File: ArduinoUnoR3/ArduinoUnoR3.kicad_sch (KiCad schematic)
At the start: 6 parts, among them U1 ATmega16U2-A, U2 LMV358

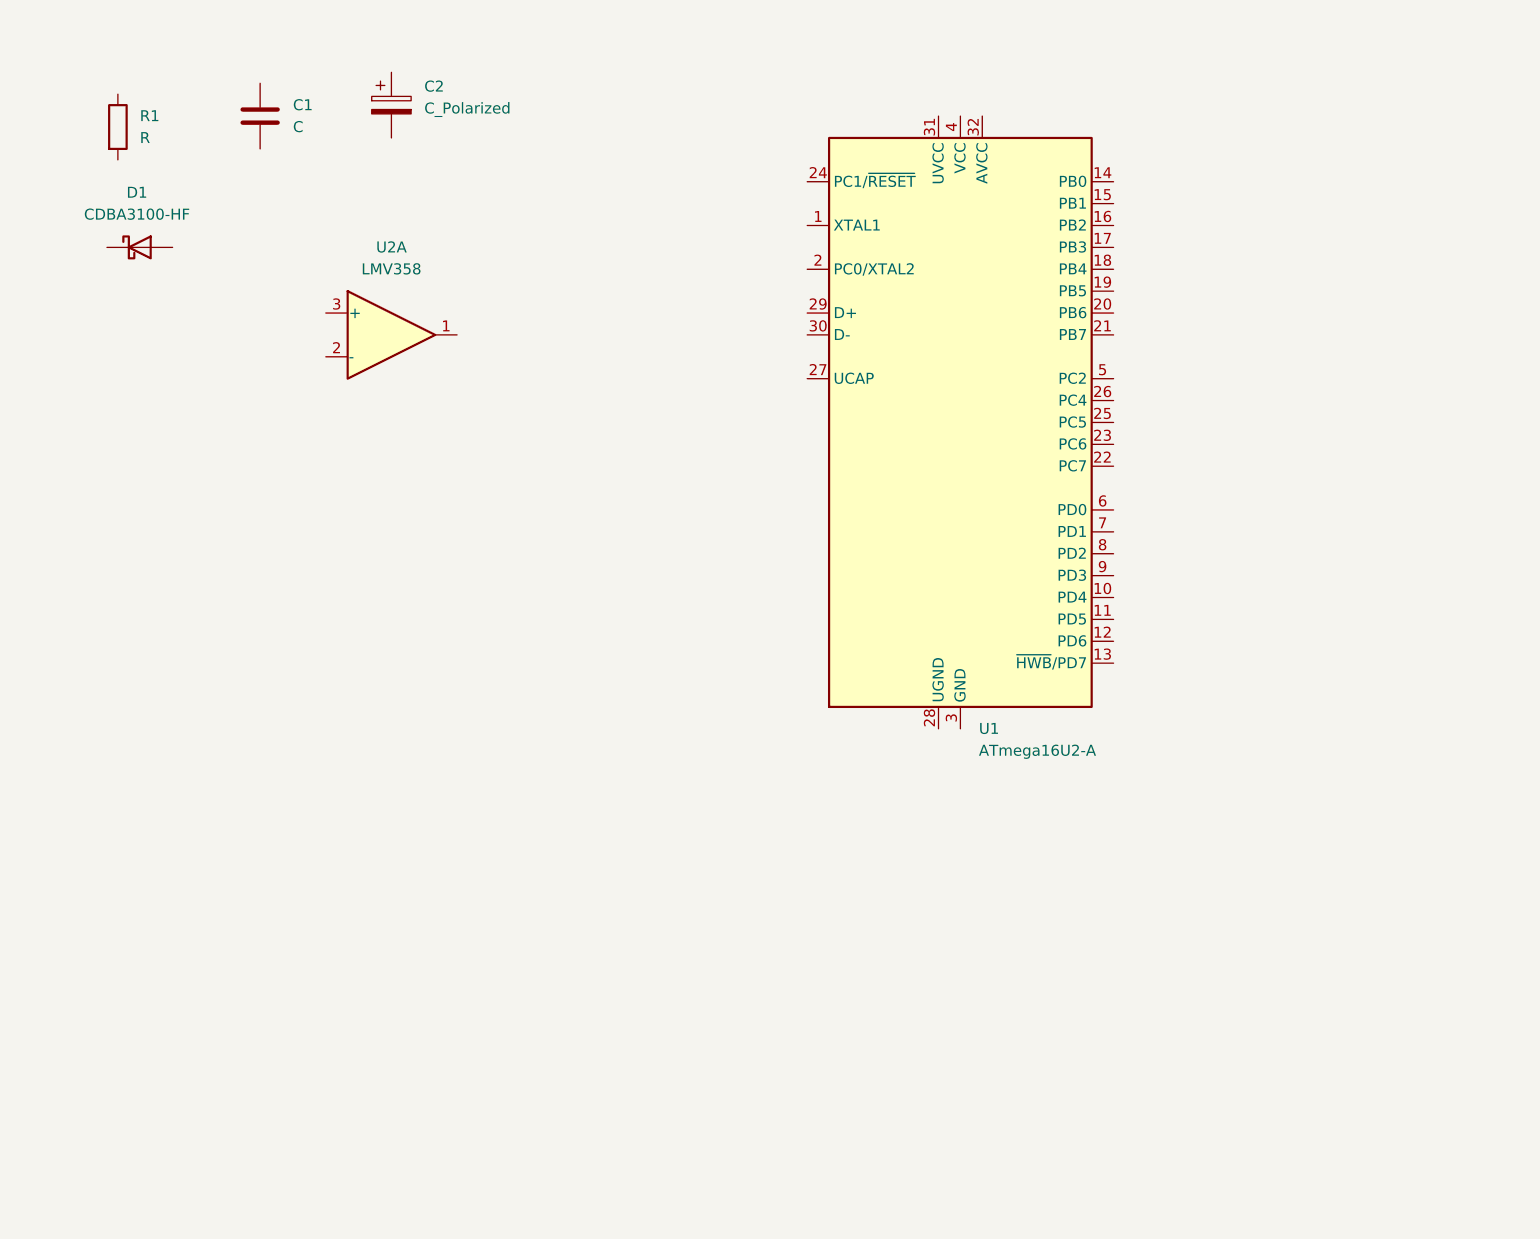
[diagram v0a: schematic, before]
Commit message: Completed the schematic design for ATMEGA16U2-A
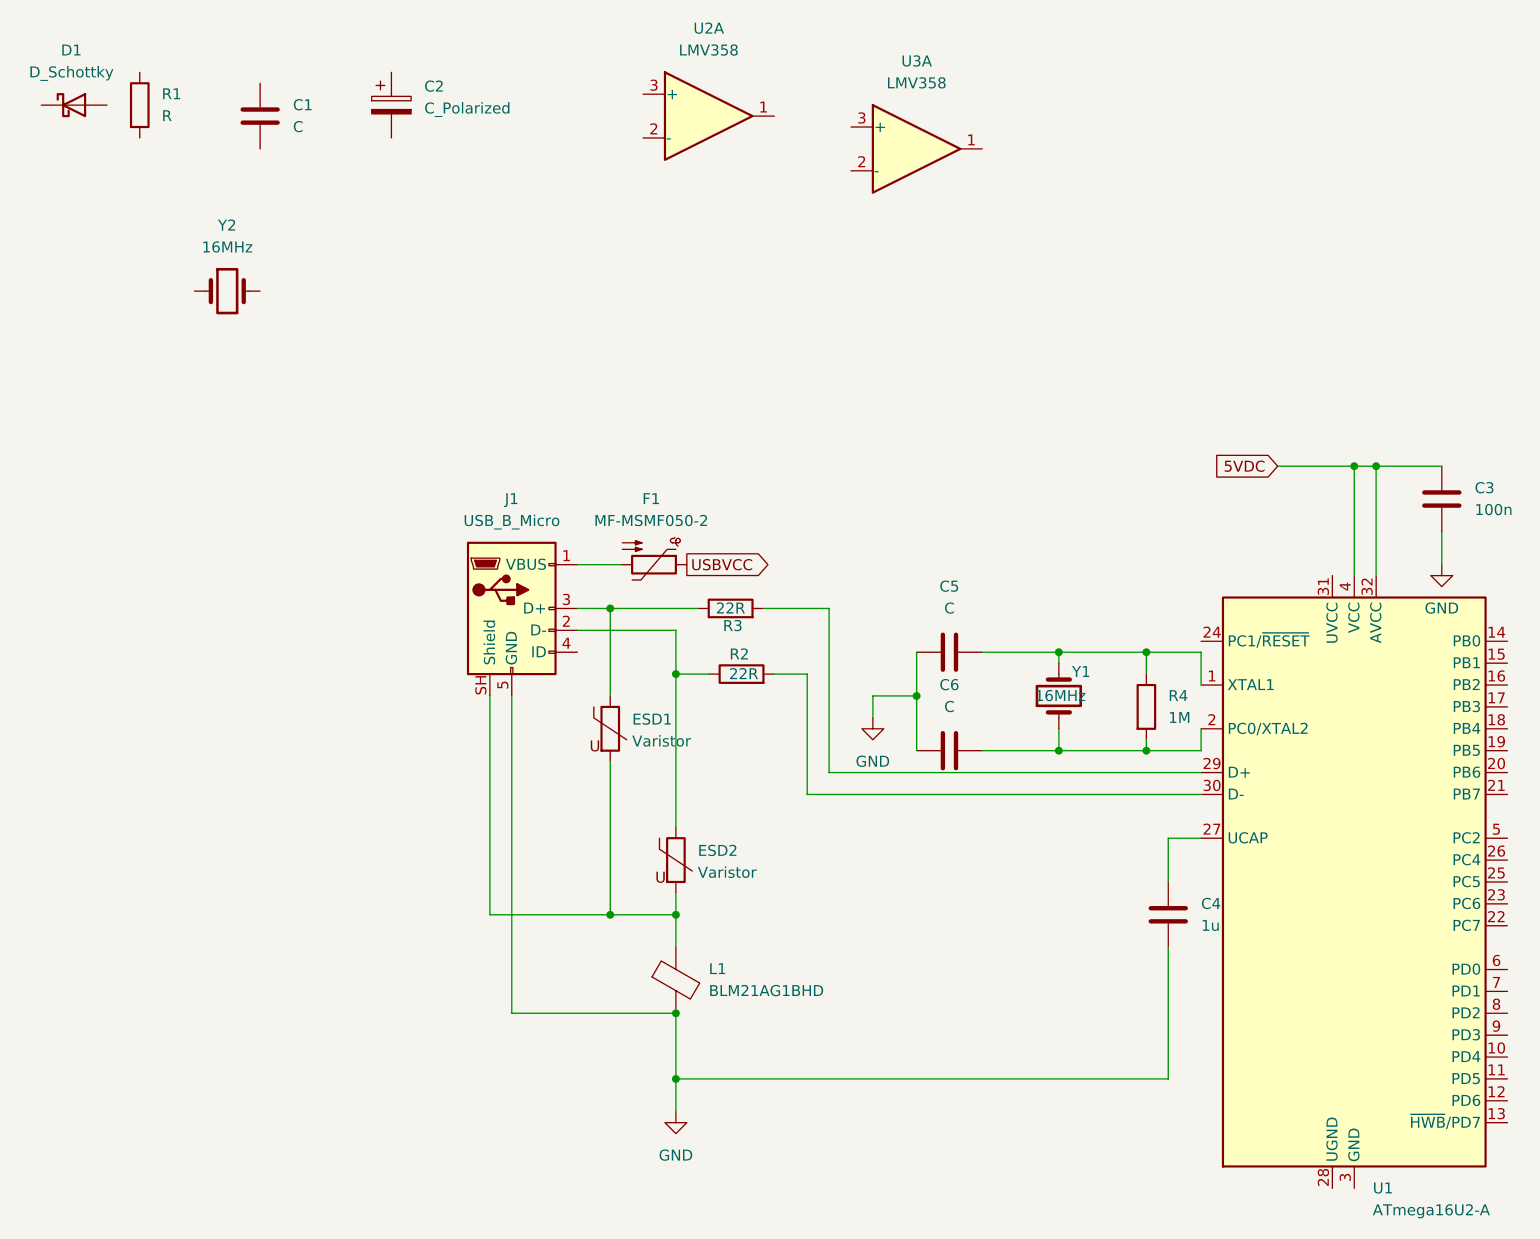
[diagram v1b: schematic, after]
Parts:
- removed D1: CDBA3100-HF, Diode_SMD:D_SMA, symbol Diode:CDBA3100-HF
- added C3: 100n, Capacitor_SMD:C_0603_1608Metric, symbol Device:C
- added C4: 1u, Capacitor_SMD:C_0603_1608Metric, symbol Device:C
- added C5, C6: C, Capacitor_SMD:C_0603_1608Metric, symbol Device:C
- added D1: D_Schottky, Diode_SMD:D_0603_1608Metric, symbol Device:D_Schottky
- added ESD1, ESD2: Varistor, symbol Device:Varistor
- added F1: MF-MSMF050-2, symbol Device:Thermistor_PTC
- added J1: USB_B_Micro, symbol Connector:USB_B_Micro
- added L1: BLM21AG1BHD, symbol Device:FerriteBead
- added R2, R3: 22R, Resistor_SMD:R_0603_1608Metric, symbol Device:R
- added R4: 1M, Resistor_SMD:R_0603_1608Metric, symbol Device:R
- added U3: LMV358, symbol Amplifier_Operational:LMV358
- added Y1, Y2: 16MHz, symbol Device:Crystal
- C1, C2: footprint Capacitor_THT:CP_Radial_D5.0mm_P2.00mm -> Capacitor_SMD:C_0603_1608Metric
- R1: footprint Resistor_THT:R_Axial_DIN0204_L3.6mm_D1.6mm_P7.62mm_Horizontal -> Resistor_SMD:R_0603_1608Metric
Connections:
- net at U1.1 (XTAL1): now also C5.2, R4.1, Y1.2
- net at U1.2 (PC0/XTAL2): now also C6.2, R4.2, Y1.1
- net at U1.27 (UCAP): now also C4.1
- net at U1.29 (D+): now also R3.2
- net at U1.30 (D-): now also R2.2
- net 5VDC: now reaches U1.32 (AVCC)
- net 5VDC: now also U1.4 (VCC), C3.1
- new net: ESD1.1, J1.3 (D+), R3.1
- new net: F1.2, J1.1 (VBUS)
- new net: ESD1.2, ESD2.2, J1.SH (Shield), L1.1
- new net: ESD2.1, J1.2 (D-), R2.1
- new net GND: C3.2, C4.2, C5.1, C6.1, J1.5 (GND), L1.2
- new net USBVCC: F1.1
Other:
- company: (none) -> Denoe
- title: (none) -> ArduinoUnoR3
- moved on the sheet: R1, U1, U2A

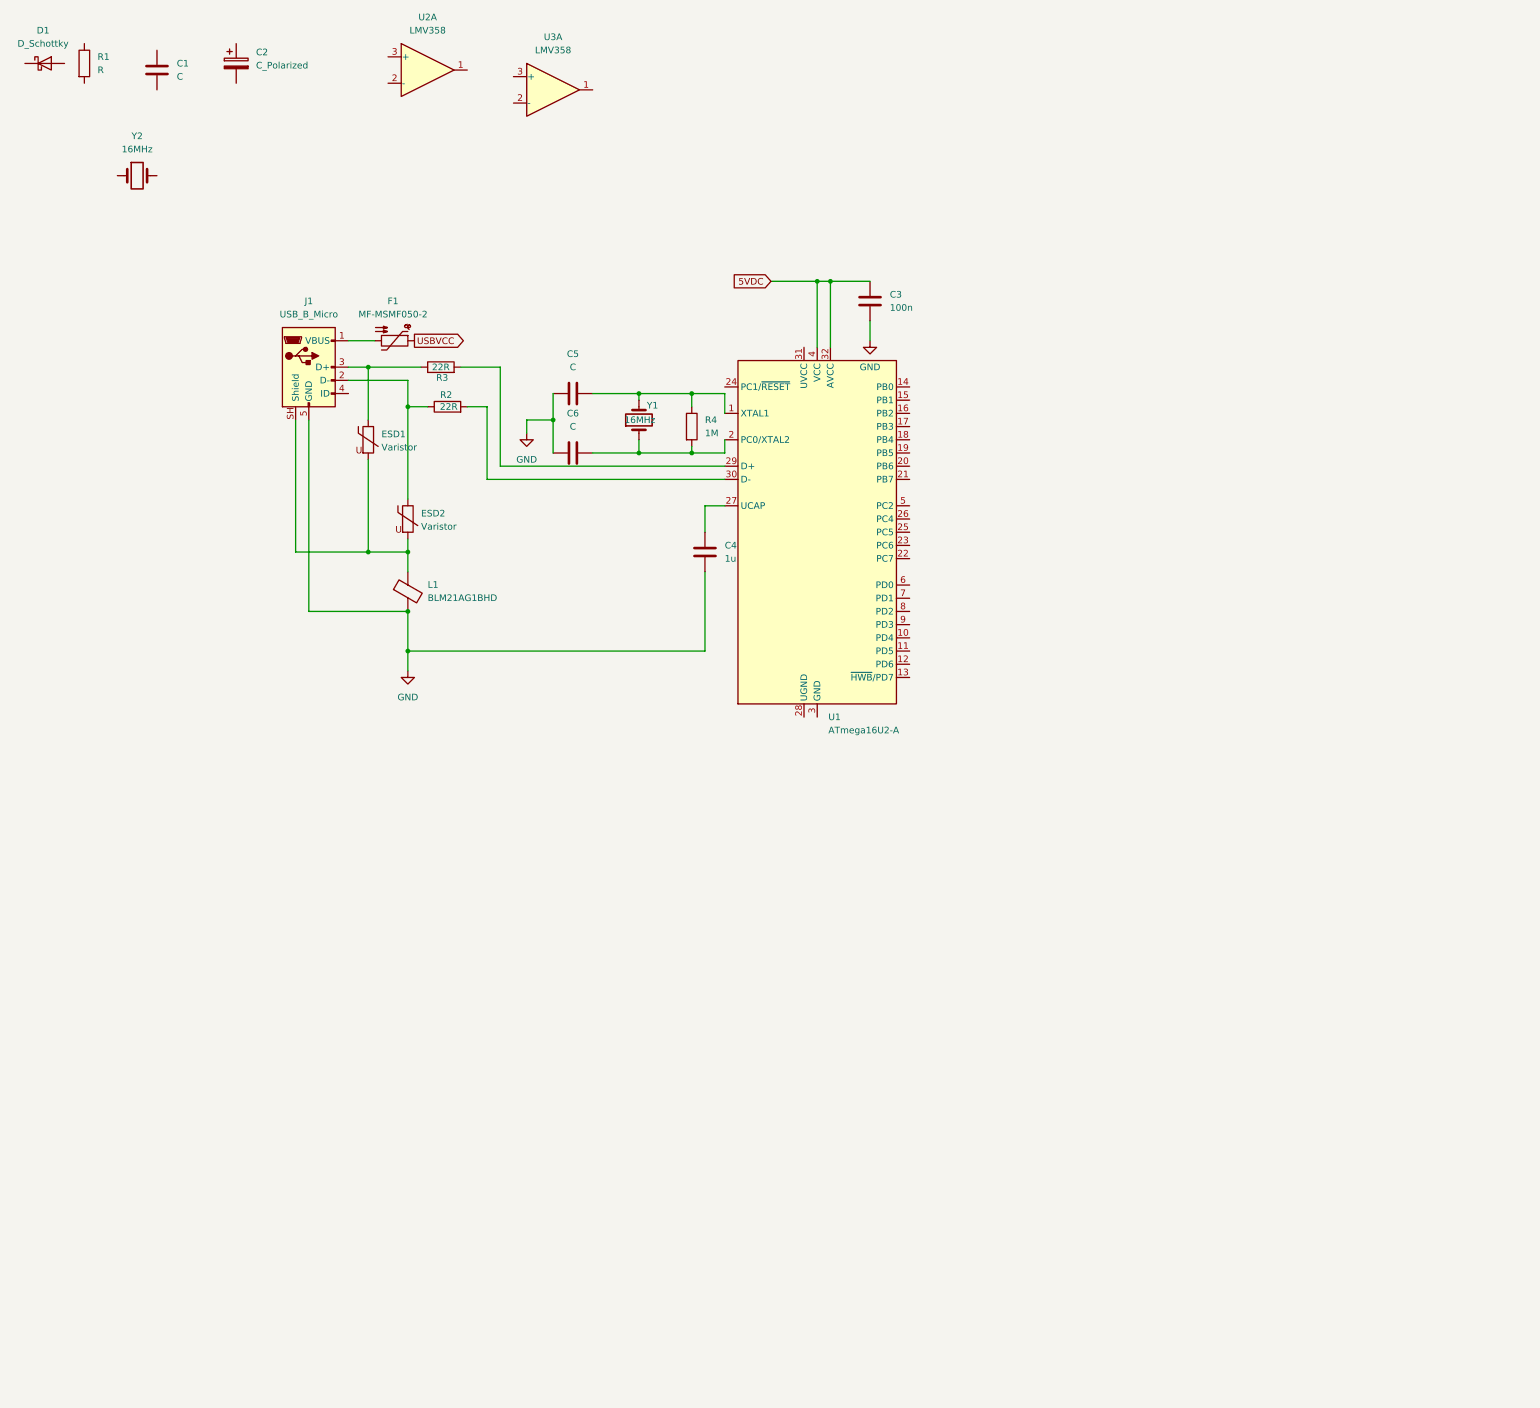
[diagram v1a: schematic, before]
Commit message: Added ATMEGA328PB-A to our schematic files
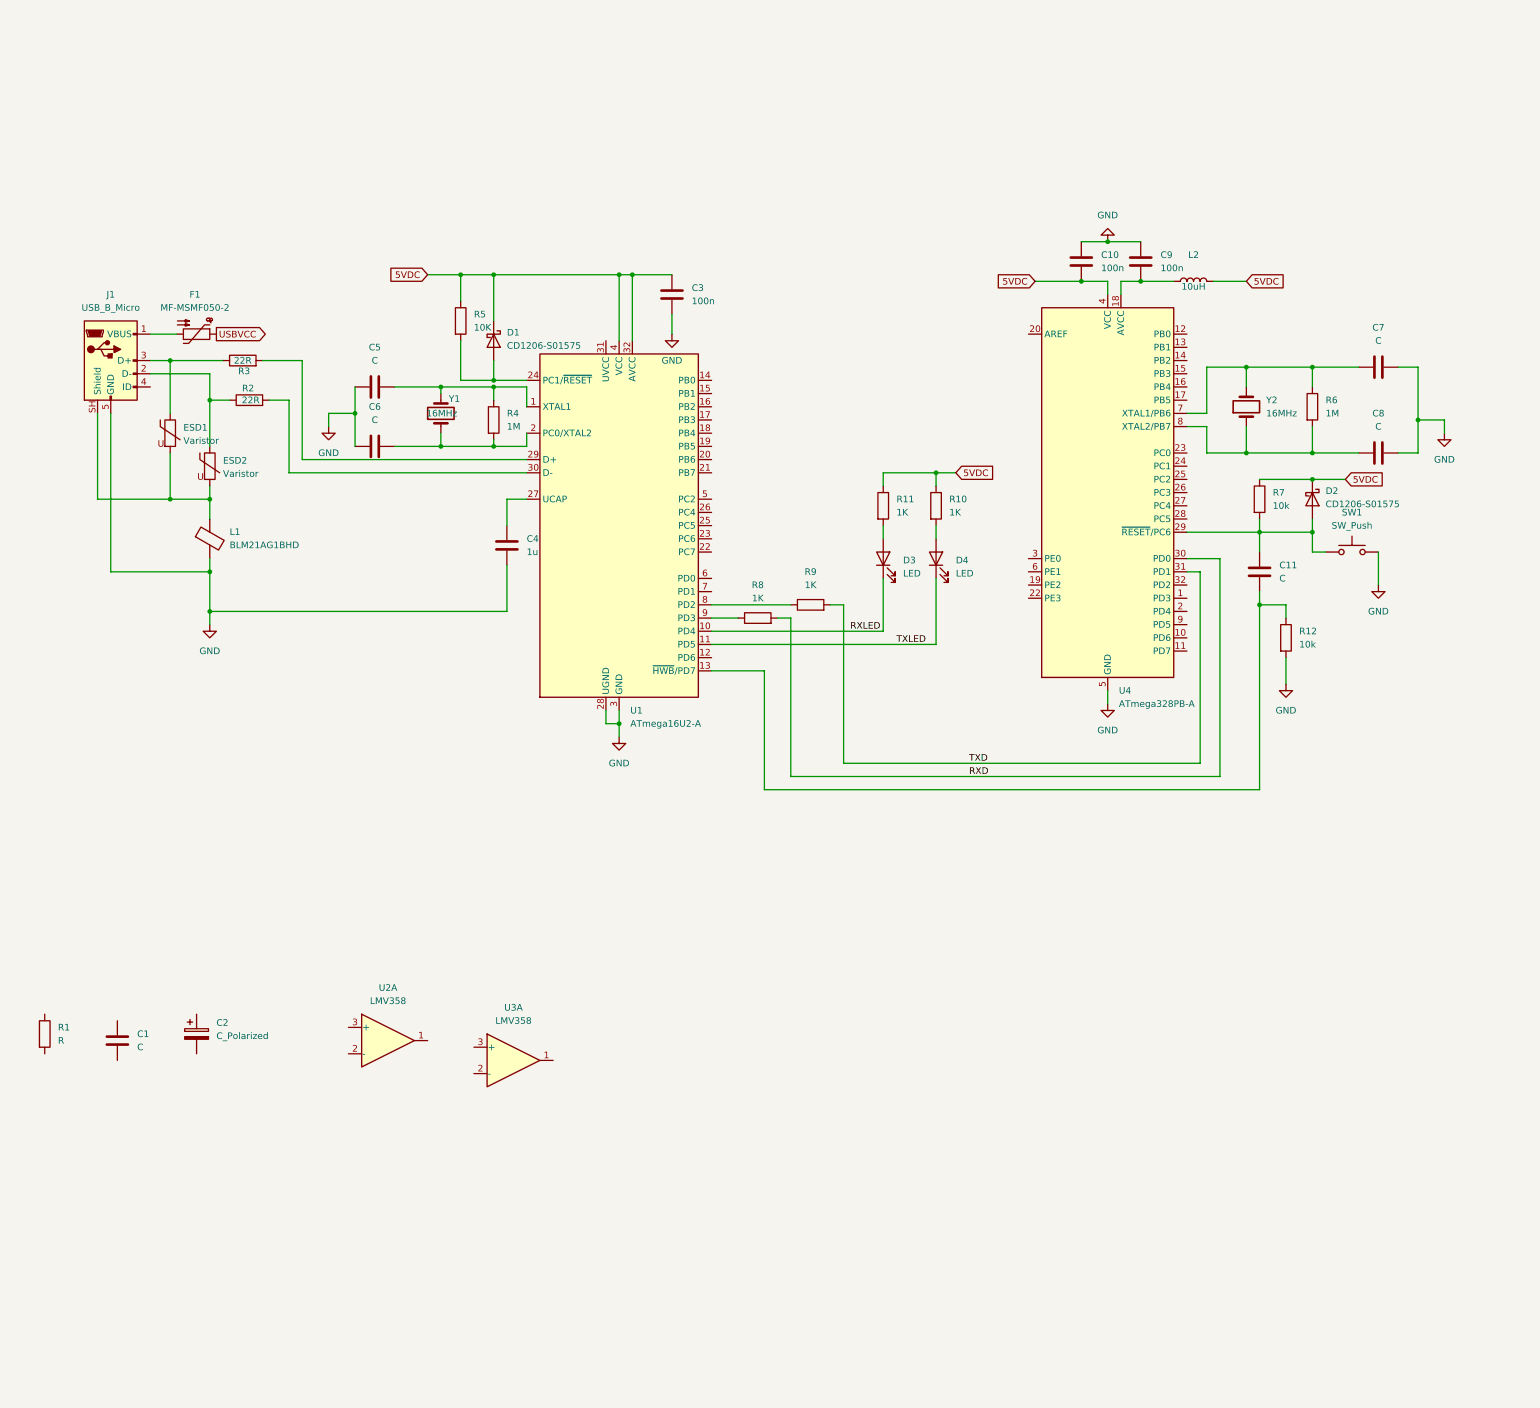
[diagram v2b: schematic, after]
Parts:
- added C10, C9: 100n, Capacitor_SMD:C_0603_1608Metric, symbol Device:C
- added C11, C7, C8: C, Capacitor_SMD:C_0603_1608Metric, symbol Device:C
- added D2: CD1206-S01575, Diode_SMD:D_0603_1608Metric, symbol Device:D_Schottky
- added D3, D4: LED, symbol Device:LED
- added L2: 10uH, symbol Device:L
- added R10, R11: 1K, symbol Device:R
- added R12, R7: 10k, Resistor_SMD:R_0603_1608Metric, symbol Device:R
- added R5: 10K, Resistor_SMD:R_0603_1608Metric, symbol Device:R
- added R6: 1M, Resistor_SMD:R_0603_1608Metric, symbol Device:R
- added R8, R9: 1K, Resistor_SMD:R_0603_1608Metric, symbol Device:R
- added SW1: SW_Push, symbol Switch:SW_Push
- added U4: ATmega328PB-A, Package_QFP:TQFP-32_7x7mm_P0.8mm, symbol MCU_Microchip_ATmega:ATmega328PB-A
- D1: value D_Schottky -> CD1206-S01575
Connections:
- net 5VDC: now also D1.1 (K), C10.2, D2.1 (K), L2.2, R10.1, R11.1, R5.1, R7.1, U4.4 (VCC)
- net GND: now also U1.28 (UGND), U1.3 (GND), C10.1, C7.2, C8.2, C9.1, R12.2, SW1.2, U4.21 (GND), U4.5 (GND)
- net at Y2.1: now also C8.1, R6.2, U4.8 (XTAL2/PB7)
- net at Y2.2: now also C7.1, R6.1, U4.7 (XTAL1/PB6)
- net RXLED: now reaches U1.10 (PD4)
- net RXLED: now also D3.1 (K)
- net TXLED: now reaches U1.11 (PD5)
- net TXLED: now also D4.1 (K)
- net at U1.13 (~{HWB}/PD7): now also C11.2, R12.1
- net at U1.24 (PC1/~{RESET}): now also D1.2 (A), R5.2
- net at U1.8 (PD2): now also R9.1
- net at U1.9 (PD3): now also R8.1
- new net: C11.1, D2.2 (A), R7.2, SW1.1, U4.29 (~{RESET}/PC6)
- new net: D4.2 (A), R10.2
- new net: D3.2 (A), R11.2
- new net: C9.2, L2.1, U4.18 (AVCC)
- new net RXD: R8.2, U4.30 (PD0)
- new net TXD: R9.2, U4.31 (PD1)
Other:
- moved on the sheet: C1, C2, C3, C4, C5, C6, D1, ESD1, ESD2, F1, J1, L1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
